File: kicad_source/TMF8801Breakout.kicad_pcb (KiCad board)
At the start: 2 copper layers, 30 x 20 mm, 27 parts, among them CN1 CONN_01X06, CN2 CONN_01X07, Q1 BSS138, Q2 BSS138, Q3 BSS138, U1 TPS736XX, U2 TMF8801

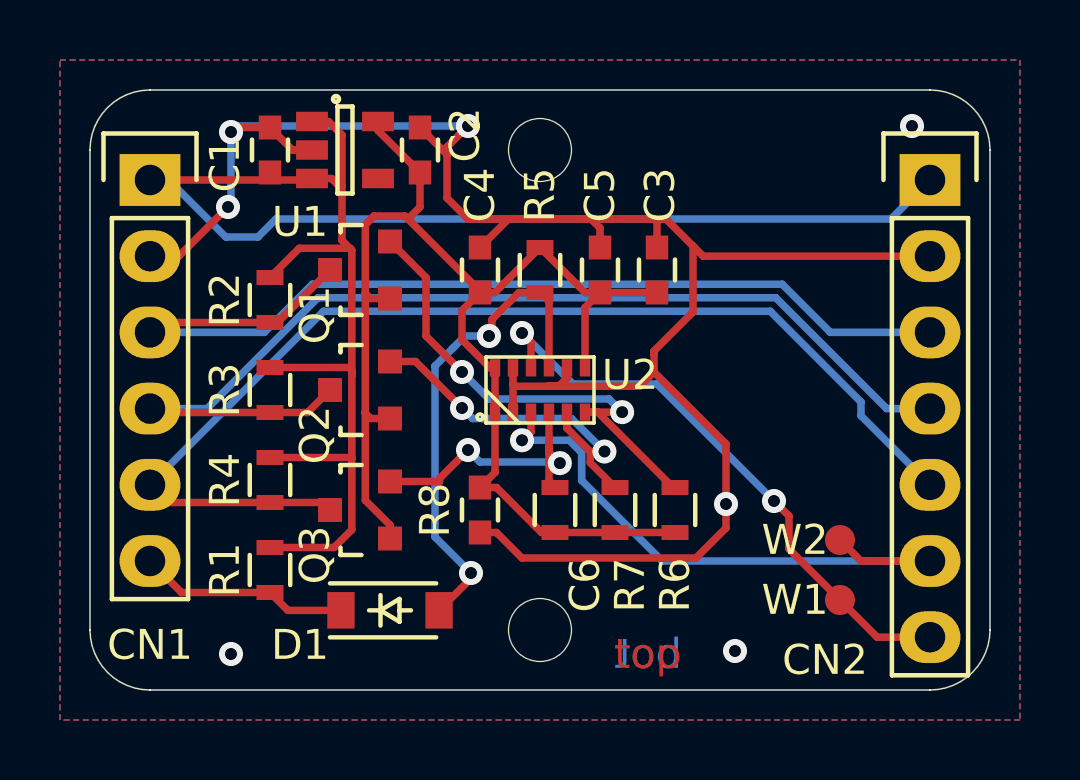
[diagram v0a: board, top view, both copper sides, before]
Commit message: added Arduino ESLOV connector
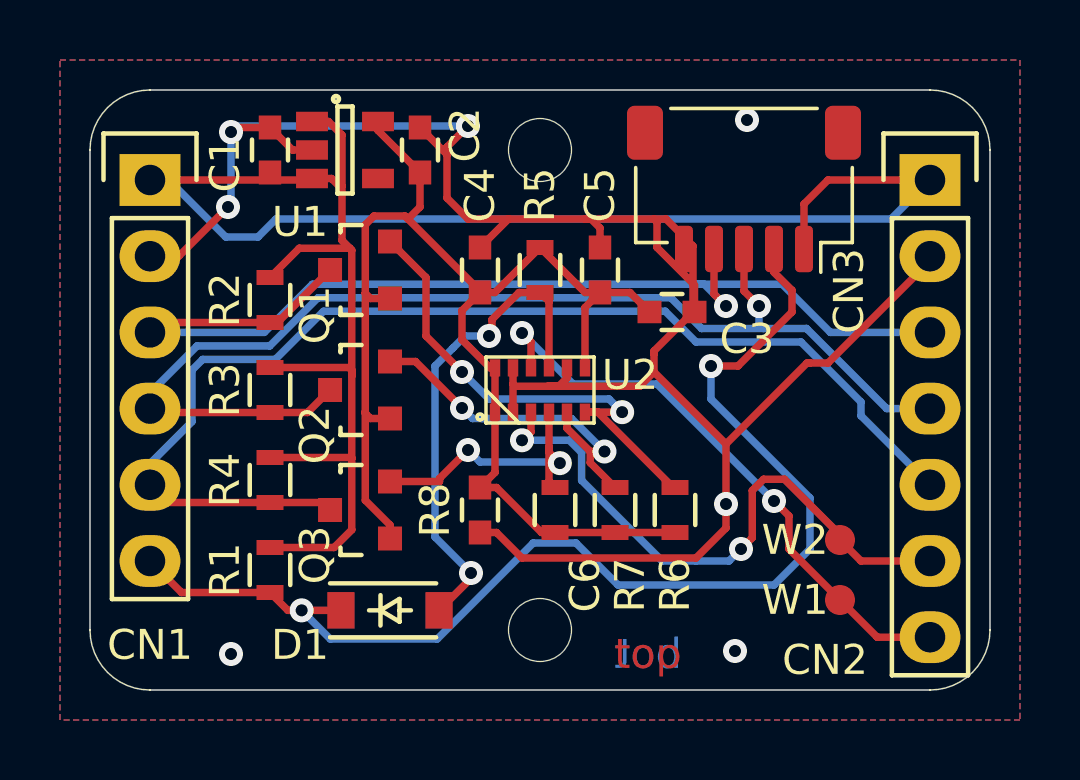
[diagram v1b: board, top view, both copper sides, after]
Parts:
- added CN3: SM05B-SRSS-TB, Connector_JST:JST_SH_SM05B-SRSS-TB_1x05-1MP_P1.00mm_Horizontal, F.Cu at (171.8, 109.3)
- L1: footprint labels:generationmake_small_solder -> labels:generationmake_small_silk; moved to B.Cu
- moved L1 12.3 mm to (165.0, 114.4), turned to 180 degrees
- moved C3 1.49 mm to (169.4, 113.4), turned to 0 degrees
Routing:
- net /EN_5V: track 7.05 -> 40.1 mm, vias 0 -> 2
- net VCC: track 60.7 -> 66.7 mm
- net GND: track 68.7 -> 72.8 mm
- net /I2C_SDA_5V: track 34.2 -> 37.8 mm, vias 0 -> 1
- net /I2C_SCL_5V: track 35.4 -> 38.7 mm, vias 0 -> 1
- net /INT_5V: track 37.4 -> 38.8 mm
- net /GPIO0: vias 1 -> 2
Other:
- board text added: "TMF8801 Breakout 0.1"
- board text removed: "TMF8801Breakout 0.1"

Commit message: moved CN1 and CN1 into 0.1 inch grid, made pcb slightly smaller, performed DRC
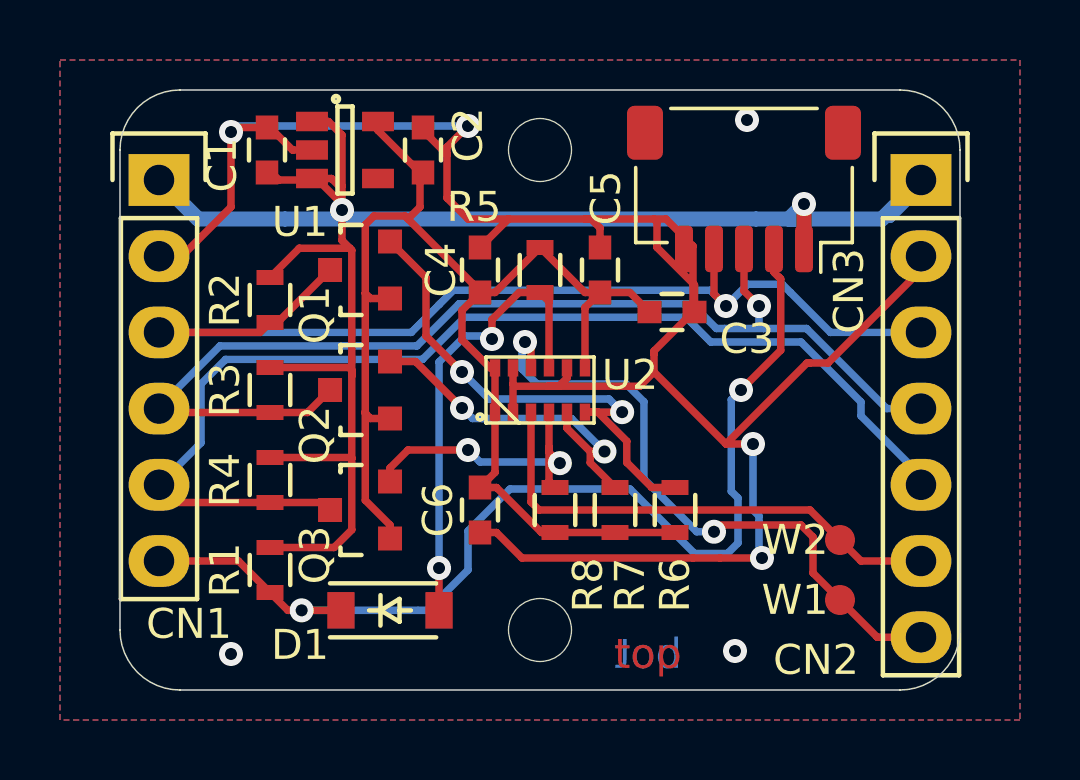
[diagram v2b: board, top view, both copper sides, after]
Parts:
- moved CN1 0.30 mm to (152.3, 109.0)
- moved CN2 0.30 mm to (177.7, 109.0)
- moved C1 0.10 mm to (155.9, 108.0)
- moved C2 0.10 mm to (161.1, 108.0)
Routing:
- net VCC: track 66.7 -> 81.9 mm, vias 0 -> 2
- net /EN_5V: track 40.1 -> 35.4 mm
- net /GPIO0: track 20.2 -> 17.1 mm, vias 2 -> 0
- net GND: track 72.8 -> 75.4 mm
- net /GPIO1: track 19.7 -> 21.7 mm
- net /I2C_SDA_5V: track 37.8 -> 36.4 mm
- net /EN: track 16.5 -> 15.5 mm
- net /INT_5V: track 38.8 -> 38.1 mm
- net /I2C_SCL_5V: track 38.7 -> 37.9 mm
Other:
- board size 30 x 20 mm -> 28 x 20 mm

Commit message: updated images
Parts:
- U1: value TPS736XX -> MIC5225-3.3
